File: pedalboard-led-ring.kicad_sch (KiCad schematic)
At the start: 11 parts, among them J1 Conn_02x03, U1 TLC5973

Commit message: Fix ERC
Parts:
- removed J1: Conn_02x03, Connector_PinHeader_2.54mm:PinHeader_2x03_P2.54mm_Vertical_SMD, symbol Connector_Generic:Conn_02x03_Top_Bottom
- added J1: Conn_02x03, symbol pedalboard-led-ring:Conn_02x03
- C1: value C_Bipolar_SMD_D5.0mm_H5.4mm -> 1uF
- C2: value C -> 100nF
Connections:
- net GND: now also J1.3 (GND), J1.4 (GND)
- net VCC: now also J1.5 (VCC)
- net VDC: now also J1.2 (VLED)
- net at U1.6 (SDI): now also J1.1 (SDI)
- net at U1.5 (SDO): now also J1.6 (SDO)
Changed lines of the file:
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@@
+    (stroke (width 0) (type default))
+  )
+  (wire (pts (xy 55.88 152.4) (xy 55.88 149.86))
     (stroke (width 0) (type default))
   )
@@
     )
   )
-  (symbol (lib_id "PCM_4ms_Power-symbol:GND") (at 128.27 129.54 0) (unit 1)
+  (symbol (lib_id "power:GND") (at 128.27 129.54 0) (unit 1)
     (in_bom yes) (on_board yes) (dnp no) (fields_autoplaced)
     (property "Reference" "#PWR08" (at 128.27 135.89 0)
@@
       (effects (font (size 1.27 1.27)) (justify left))
     )
-    (property "Value" "C_Bipolar_SMD_D5.0mm_H5.4mm" (at 214.63 41.275 0)
+    (property "Value" "1uF" (at 214.63 41.275 0)
       (effects (font (size 1.27 1.27)) (justify left))
     )
@@
     )
   )
-  (symbol (lib_id "power:GND") (at 55.88 149.86 0) (unit 1)
-    (in_bom yes) (on_board yes) (dnp no) (fields_autoplaced)
-    (property "Reference" "#PWR01" (at 55.88 156.21 0)
-      (effects (font (size 1.27 1.27)) hide)
-    )
-    (property "Value" "GND" (at 55.88 154.94 0)
-      (effects (font (size 1.27 1.27)))
-    )
-    (property "Footprint" "" (at 55.88 149.86 0)
-      (effects (font (size 1.27 1.27)) hide)
-    )
-    (property "Datasheet" "" (at 55.88 149.86 0)
+  (symbol (lib_id "power:GND") (at 55.88 152.4 0) (unit 1)
+    (in_bom yes) (on_board yes) (dnp no) (fields_autoplaced)
+    (property "Reference" "#PWR01" (at 55.88 158.75 0)
+      (effects (font (size 1.27 1.27)) hide)
+    )
+    (property "Value" "GND" (at 55.88 157.48 0)
+      (effects (font (size 1.27 1.27)))
+    )
+    (property "Footprint" "" (at 55.88 152.4 0)
+      (effects (font (size 1.27 1.27)) hide)
+    )
+    (property "Datasheet" "" (at 55.88 152.4 0)
       (effects (font (size 1.27 1.27)) hide)
     )
@@
     )
   )
-  (symbol (lib_id "Connector_Generic:Conn_02x03_Top_Bottom") (at 54.61 138.43 0) (unit 1)
-    (in_bom yes) (on_board yes) (dnp no) (fields_autoplaced)
-    (property "Reference" "J1" (at 55.88 130.81 0)
-      (effects (font (size 1.27 1.27)))
-    )
-    (property "Value" "Conn_02x03" (at 55.88 133.35 0)
-      (effects (font (size 1.27 1.27)))
-    )
-    (property "Footprint" "Connector_PinHeader_2.54mm:PinHeader_2x03_P2.54mm_Vertical_SMD" (at 54.61 138.43 0)
-      (effects (font (size 1.27 1.27)) hide)
-    )
-    (property "Datasheet" "~" (at 54.61 138.43 0)
-      (effects (font (size 1.27 1.27)) hide)
-    )
-    (pin "1")
-    (pin "2")
-    (pin "3")
-    (pin "4")
-    (pin "5")
-    (pin "6")
-    (instances
-      (project "pedalboard-led-ring"
-        (path "/02aefeb1-bdda-4e04-a64a-6cb1fcf66702"
-          (reference "J1") (unit 1)
-        )
-      )
-    )
-  )
   (symbol (lib_id "pedalboard-led-ring:RGB-LED") (at 191.77 92.71 270) (unit 1)
     (in_bom yes) (on_board yes) (dnp no) (fields_autoplaced)
@@
       (effects (font (size 1.27 1.27)) (justify left))
     )
-    (property "Value" "C" (at 132.08 126.365 0)
+    (property "Value" "100nF" (at 132.08 126.365 0)
       (effects (font (size 1.27 1.27)) (justify left))
     )
@@
     )
   )
-  (symbol (lib_id "PCM_4ms_Power-symbol:GND") (at 210.82 43.18 0) (unit 1)
+  (symbol (lib_id "pedalboard-led-ring:Conn_02x03") (at 54.61 138.43 0) (unit 1)
+    (in_bom yes) (on_board yes) (dnp no) (fields_autoplaced)
+    (property "Reference" "J1" (at 55.88 130.81 0)
+      (effects (font (size 1.27 1.27)))
+    )
+    (property "Value" "Conn_02x03" (at 55.88 133.35 0)
+      (effects (font (size 1.27 1.27)))
+    )
+    (property "Footprint" "" (at 54.61 138.43 0)
+      (effects (font (size 1.27 1.27)) hide)
+    )
+    (property "Datasheet" "~" (at 54.61 138.43 0)
+      (effects (font (size 1.27 1.27)) hide)
+    )
+    (pin "1")
+    (pin "2")
+    (pin "3")
+    (pin "4")
+    (pin "5")
+    (pin "6")
+    (instances
+      (project "pedalboard-led-ring"
+        (path "/02aefeb1-bdda-4e04-a64a-6cb1fcf66702"
+          (reference "J1") (unit 1)
+        )
+      )
+    )
+  )
+  (symbol (lib_id "power:GND") (at 210.82 43.18 0) (unit 1)
     (in_bom yes) (on_board yes) (dnp no) (fields_autoplaced)
     (property "Reference" "#PWR07" (at 210.82 49.53 0)

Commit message: First routing
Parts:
- C2: footprint Capacitor_SMD:C_01005_0402Metric_Pad0.57x0.30mm_HandSolder -> Capacitor_SMD:C_0504_1310Metric_Pad0.83x1.28mm_HandSolder
- J1: footprint (none) -> Connector_PinHeader_2.54mm:PinHeader_2x03_P2.54mm_Vertical_SMD
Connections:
- net GND: now also J1.5 (GND), J1.6 (GND); no longer J1.3 (GND), J1.4 (GND)
- net VCC: now also J1.4 (VCC); no longer J1.5 (VCC)
- net VDC: now also J1.3 (VLED); no longer J1.2 (VLED)
- net at U1.5 (SDO): now also J1.2 (SDO); no longer J1.6 (SDO)
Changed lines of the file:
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@@
       (effects (font (size 1.27 1.27)) (justify left))
     )
-    (property "Footprint" "Capacitor_SMD:C_01005_0402Metric_Pad0.57x0.30mm_HandSolder" (at 129.2352 128.27 0)
+    (property "Footprint" "Capacitor_SMD:C_0504_1310Metric_Pad0.83x1.28mm_HandSolder" (at 129.2352 128.27 0)
       (effects (font (size 1.27 1.27)) hide)
     )
@@
       (effects (font (size 1.27 1.27)))
     )
-    (property "Footprint" "" (at 54.61 138.43 0)
+    (property "Footprint" "Connector_PinHeader_2.54mm:PinHeader_2x03_P2.54mm_Vertical_SMD" (at 54.61 138.43 0)
       (effects (font (size 1.27 1.27)) hide)
     )

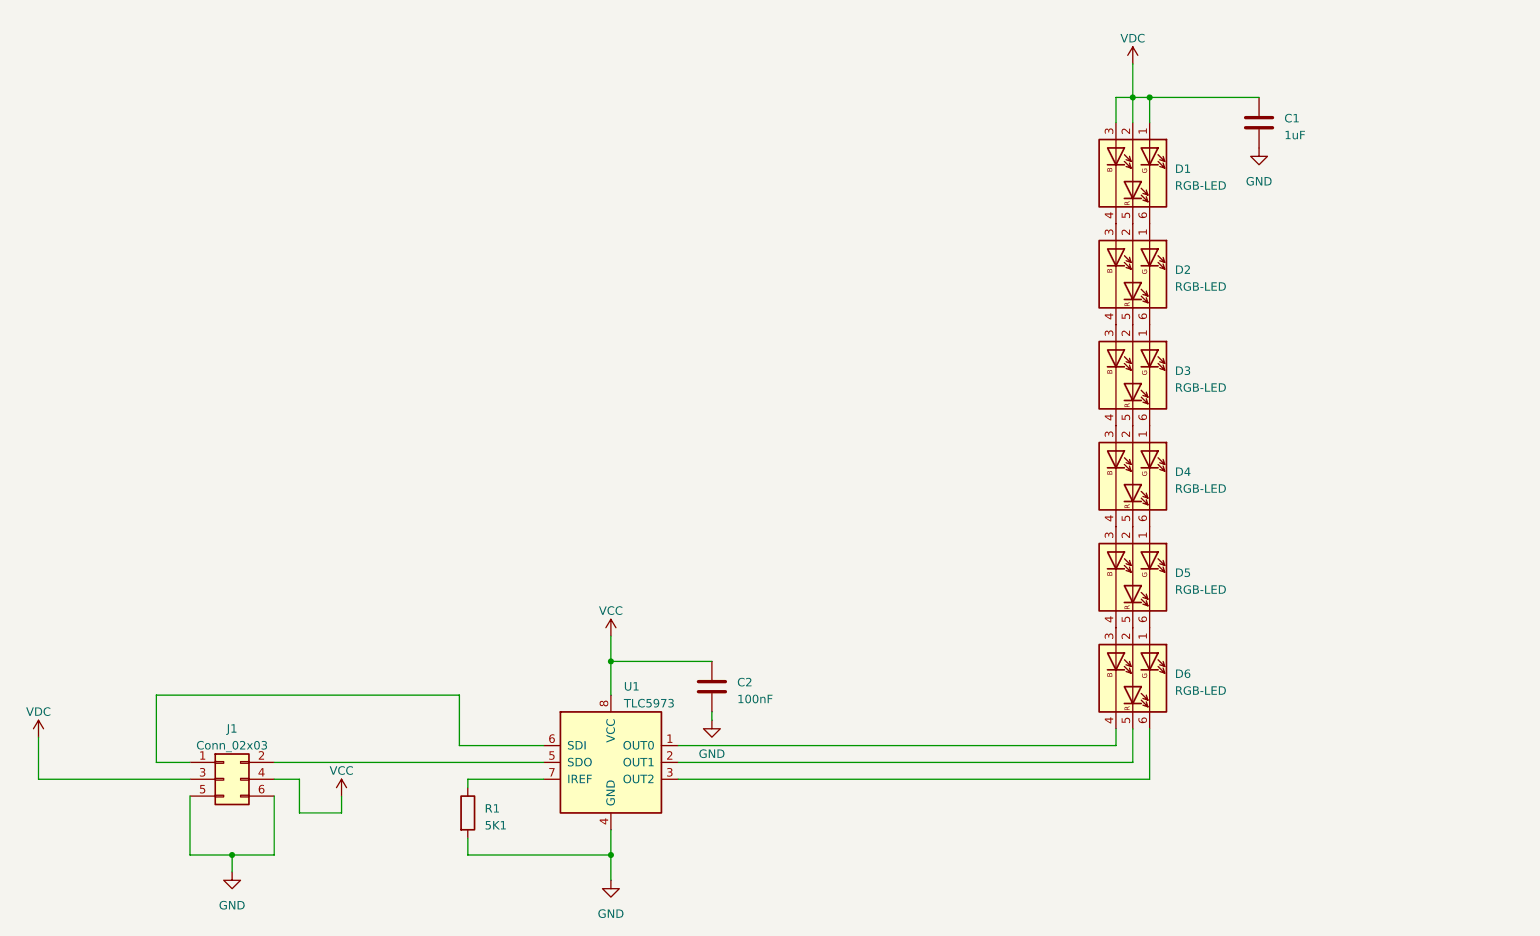
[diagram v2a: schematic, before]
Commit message: First version of the PSU
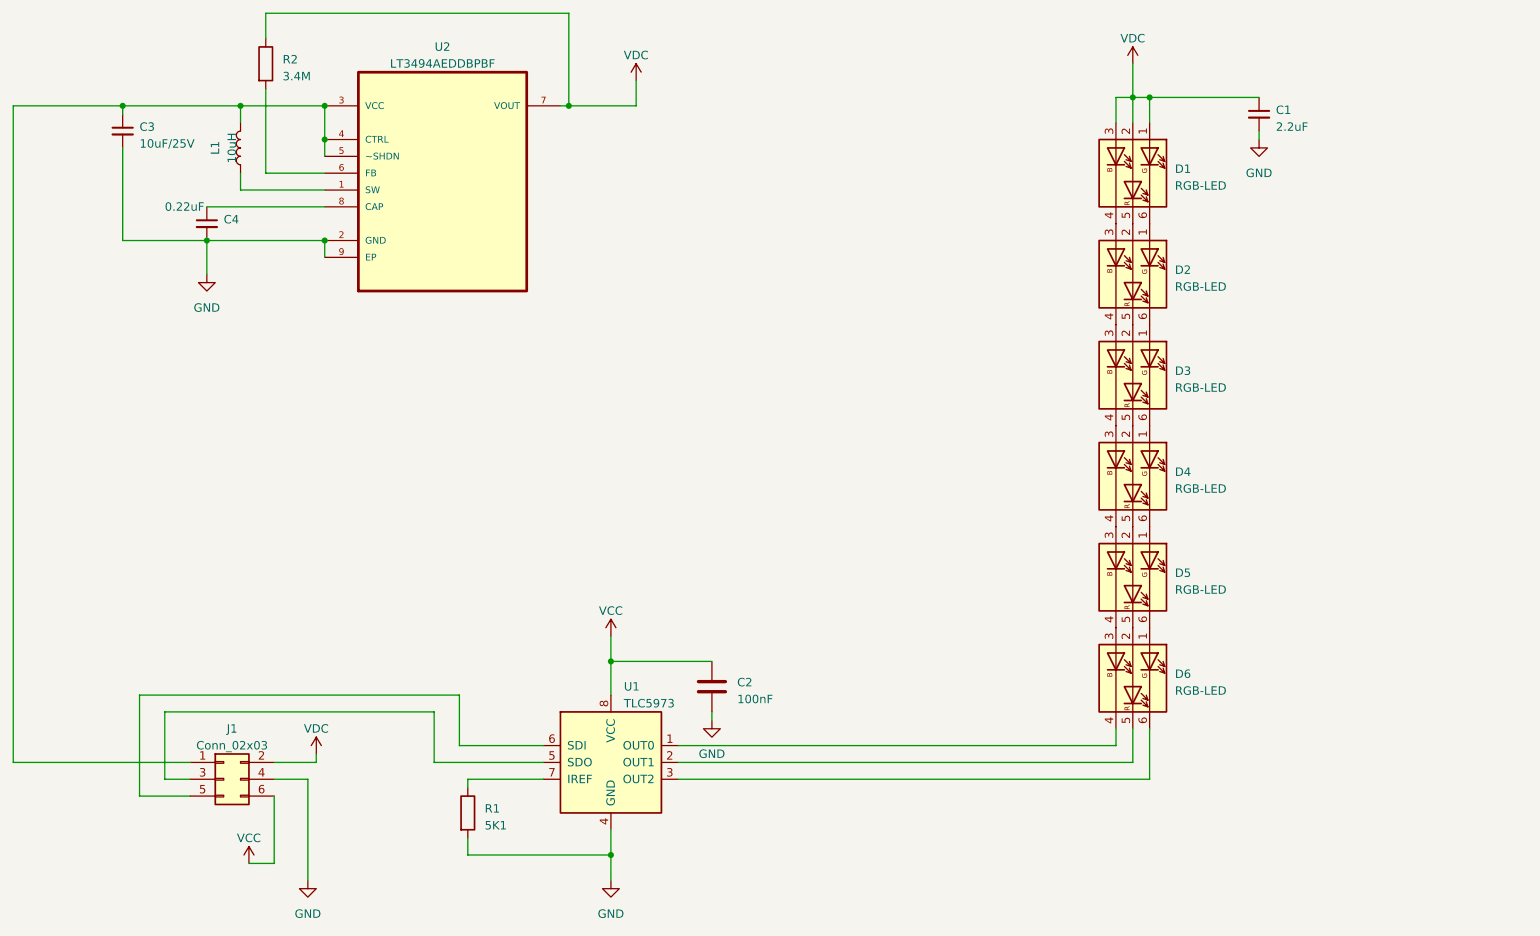
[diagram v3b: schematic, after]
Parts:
- removed C1: 1uF, PCM_Capacitor_SMD_AKL:C_Elec_5x5.4, symbol PCM_Capacitor_AKL:C_Bipolar_SMD_D5.0mm_H5.4mm
- added C1: 2.2uF_0603_25V, Capacitor_SMD:C_0201_0603Metric, symbol PCM_4ms_Capacitor:2.2uF_0603_25V
- added C3: 10uF_0805_25V, Capacitor_SMD:C_0805_2012Metric, symbol PCM_4ms_Capacitor:10uF_0805_25V
- added C4: 0.22uF_0603_25V, Capacitor_SMD:C_0201_0603Metric, symbol PCM_4ms_Capacitor:0.22uF_0603_25V
- added L1: 10uH, Library:IND_LQH32CN150K53L, symbol Device:L
- added R2: 3.4M, PCM_4ms_Resistor:R_0603, symbol PCM_Resistor_AKL:R_0805
- added U2: LT3494AEDDBPBF, DFN300X200X80-9N, symbol pedalboard-led-ring:LT3494AEDDBPBF
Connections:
- net GND: now also J1.4 (VCC), C1.2, C3.2, C4.2, U2.2 (GND), U2.9 (EP); no longer J1.5 (GND), J1.6 (GND)
- net VCC: now also J1.6 (GND); no longer J1.4 (VCC)
- net VDC: now also J1.2 (SDO), C1.1, R2.1, U2.7 (VOUT); no longer J1.3 (VLED)
- net at U1.5 (SDO): now also J1.3 (VLED); no longer J1.2 (SDO)
- net at J1.1 (SDI): now also C3.1, L1.2, U2.3 (VCC), U2.4 (CTRL), U2.5 (~SHDN); no longer U1.6 (SDI)
- new net: L1.1, U2.1 (SW)
- new net: C4.1, U2.8 (CAP)
- new net: J1.5 (GND), U1.6 (SDI)
- new net: R2.2, U2.6 (FB)

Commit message: PSU improved
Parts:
- C1: footprint Capacitor_SMD:C_0201_0603Metric -> Capacitor_SMD:C_1206_3216Metric_Pad1.33x1.80mm_HandSolder
- C2: footprint Capacitor_SMD:C_0504_1310Metric_Pad0.83x1.28mm_HandSolder -> Capacitor_SMD:C_0805_2012Metric_Pad1.18x1.45mm_HandSolder
- C3: footprint Capacitor_SMD:C_0805_2012Metric -> Capacitor_SMD:C_1206_3216Metric_Pad1.33x1.80mm_HandSolder
- C4: footprint Capacitor_SMD:C_0201_0603Metric -> Capacitor_SMD:C_0805_2012Metric_Pad1.18x1.45mm_HandSolder
- J1: footprint Connector_PinHeader_2.54mm:PinHeader_2x03_P2.54mm_Vertical_SMD -> Connector_PinSocket_2.54mm:PinSocket_2x03_P2.54mm_Vertical_SMD
- U2: footprint DFN300X200X80-9N -> Package_DFN_QFN:DFN-8-1EP_2x3mm_P0.5mm_EP0.61x2.2mm
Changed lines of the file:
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@@
       (effects (font (size 1.27 1.27)) hide)
     )
-    (property "Footprint" "Capacitor_SMD:C_0201_0603Metric" (at 219.075 50.8 0)
+    (property "Footprint" "Capacitor_SMD:C_1206_3216Metric_Pad1.33x1.80mm_HandSolder" (at 219.075 50.8 0)
       (effects (font (size 1.27 1.27)) hide)
     )
@@
       (effects (font (size 1.27 1.27)) hide)
     )
-    (property "Footprint" "Capacitor_SMD:C_0805_2012Metric" (at 36.83 45.72 0)
-      (effects (font (size 1.27 1.27)) (justify left) hide)
-    )
-    (property "Datasheet" "" (at 39.37 40.64 0)
+    (property "Footprint" "Capacitor_SMD:C_1206_3216Metric_Pad1.33x1.80mm_HandSolder" (at 36.83 45.72 0)
+      (effects (font (size 1.27 1.27)) (justify left) hide)
+    )
+    (property "Datasheet" "https://search.murata.co.jp/Ceramy/image/img/A01X/G101/ENG/GRM21BR61E106MA73-01.pdf" (at 39.37 40.64 0)
       (effects (font (size 1.27 1.27)) hide)
     )
@@
       (effects (font (size 1.27 1.27)) hide)
     )
-    (property "Footprint" "Capacitor_SMD:C_0201_0603Metric" (at 49.53 59.69 0)
+    (property "Footprint" "Capacitor_SMD:C_0805_2012Metric_Pad1.18x1.45mm_HandSolder" (at 49.53 59.69 0)
       (effects (font (size 1.27 1.27)) (justify left) hide)
     )
@@
       (effects (font (size 1.27 1.27)) (justify left))
     )
-    (property "Footprint" "Capacitor_SMD:C_0504_1310Metric_Pad0.83x1.28mm_HandSolder" (at 129.2352 128.27 0)
+    (property "Footprint" "Capacitor_SMD:C_0805_2012Metric_Pad1.18x1.45mm_HandSolder" (at 129.2352 128.27 0)
       (effects (font (size 1.27 1.27)) hide)
     )
@@
       (effects (font (size 1.27 1.27)))
     )
-    (property "Footprint" "Connector_PinHeader_2.54mm:PinHeader_2x03_P2.54mm_Vertical_SMD" (at 54.61 138.43 0)
+    (property "Footprint" "Connector_PinSocket_2.54mm:PinSocket_2x03_P2.54mm_Vertical_SMD" (at 54.61 138.43 0)
       (effects (font (size 1.27 1.27)) hide)
     )
@@
       (effects (font (size 1.27 1.27)))
     )
-    (property "Footprint" "DFN300X200X80-9N" (at 87.63 44.45 0)
+    (property "Footprint" "Package_DFN_QFN:DFN-8-1EP_2x3mm_P0.5mm_EP0.61x2.2mm" (at 87.63 44.45 0)
       (effects (font (size 1.27 1.27)) (justify bottom) hide)
     )

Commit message: ERC Check fixes
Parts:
- U2: footprint Package_DFN_QFN:DFN-8-1EP_2x3mm_P0.5mm_EP0.61x2.2mm -> DFN300X200X80-9N
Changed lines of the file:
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@@
       (effects (font (size 1.27 1.27)))
     )
-    (property "Footprint" "Package_DFN_QFN:DFN-8-1EP_2x3mm_P0.5mm_EP0.61x2.2mm" (at 87.63 44.45 0)
+    (property "Footprint" "DFN300X200X80-9N" (at 87.63 44.45 0)
       (effects (font (size 1.27 1.27)) (justify bottom) hide)
     )
